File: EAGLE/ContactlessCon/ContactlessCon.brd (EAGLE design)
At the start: 57.1 x 31.4 mm, 5 parts, among them J1 PINHEADER-212*1, J2 PINHEADER-818*1, X1 0446200002

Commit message: Conの配線終了
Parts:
- moved X1 5.06 mm to (30.0, 31.7)
- moved J1 2.00 mm to (6.35, 7.08)
- moved J2 1.43 mm to (53.5, 8.89)
- moved R1 1.00 mm to (28.2, 5.08)
- moved R2 1.00 mm to (28.2, 7.62)
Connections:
- net GPIO: now also X1.5; no longer X1.3
- net SCL: now also X1.4; no longer X1.5
- net SDA: now also X1.3; no longer X1.4
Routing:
- net SDA: track 0.00 -> 48.4 mm
- net SCL: track 0.00 -> 44.0 mm
- net GPIO: track 0.00 -> 40.3 mm
- net SPEAKER: track 0.00 -> 29.1 mm
- net +3V3: track 0.00 -> 22.9 mm
- added copper zone on layer 16, net GND
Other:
- board size 57.1 x 31.4 mm -> 60 x 37.1 mm
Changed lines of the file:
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@@
 <board>
 <plain>
-<wire x1="0" y1="0" x2="57.13" y2="0" width="0" layer="20"/>
-<wire x1="57.13" y1="0" x2="57.13" y2="31.42" width="0" layer="20"/>
-<wire x1="57.13" y1="31.42" x2="0" y2="31.42" width="0" layer="20"/>
-<wire x1="0" y1="31.42" x2="0" y2="0" width="0" layer="20"/>
+<wire x1="0" y1="32.1" x2="0" y2="5" width="0" layer="20"/>
+<wire x1="0" y1="5" x2="5" y2="0" width="0" layer="20" curve="90"/>
+<wire x1="5" y1="0" x2="55" y2="0" width="0" layer="20"/>
+<wire x1="55" y1="0" x2="60" y2="5" width="0" layer="20" curve="90"/>
+<wire x1="60" y1="5" x2="60" y2="32.1" width="0" layer="20"/>
+<wire x1="60" y1="32.1" x2="55" y2="37.1" width="0" layer="20" curve="90"/>
+<wire x1="55" y1="37.1" x2="5" y2="37.1" width="0" layer="20"/>
+<wire x1="5" y1="37.1" x2="0" y2="32.1" width="0" layer="20" curve="90"/>
 </plain>
 <attributes>
@@
 </autorouter>
 <elements>
-<element name="J1" library="PINHEADER" package="PINHEADER-2*1" value="PINHEADER-212*1" x="6.35" y="5.08" smashed="yes" rot="R270">
-<attribute name="NAME" x="8.255" y="7.62" size="1.016" layer="21" font="vector" ratio="15" rot="R270"/>
-</element>
-<element name="J2" library="PINHEADER" package="PINHEADER-8*1" value="PINHEADER-818*1" x="52.07" y="8.89" smashed="yes" rot="R90">
-<attribute name="NAME" x="50.165" y="1.27" size="1.016" layer="25" font="vector" ratio="15" rot="R90"/>
-</element>
-<element name="R1" library="rcl" library_urn="urn:adsk.eagle:library:334" package="R1206" package3d_urn="urn:adsk.eagle:package:23540/2" value="" x="29.21" y="5.08" smashed="yes" rot="R180">
-<attribute name="NAME" x="30.48" y="3.81" size="1.27" layer="25" rot="R180"/>
-<attribute name="POPULARITY" value="41" x="13.97" y="34.29" size="1.778" layer="27" rot="R180" display="off"/>
-<attribute name="SPICEPREFIX" value="R" x="13.97" y="34.29" size="1.778" layer="27" rot="R180" display="off"/>
-<attribute name="VALUE" x="30.48" y="7.62" size="1.27" layer="27" rot="R180"/>
-</element>
-<element name="R2" library="rcl" library_urn="urn:adsk.eagle:library:334" package="R1206" package3d_urn="urn:adsk.eagle:package:23540/2" value="" x="29.21" y="7.62" smashed="yes" rot="R180">
-<attribute name="NAME" x="27.94" y="8.89" size="1.27" layer="25"/>
-<attribute name="POPULARITY" value="41" x="8.89" y="36.83" size="1.778" layer="27" rot="R180" display="off"/>
-<attribute name="SPICEPREFIX" value="R" x="8.89" y="36.83" size="1.778" layer="27" rot="R180" display="off"/>
-<attribute name="VALUE" x="30.48" y="10.16" size="1.27" layer="27" rot="R180"/>
-</element>
-<element name="X1" library="con-molex" library_urn="urn:adsk.eagle:library:165" package="0446200002" package3d_urn="urn:adsk.eagle:package:8078921/1" value="0446200002" x="29.21" y="26.67" smashed="yes" rot="R180">
-<attribute name="MF" value="MOLEX" x="6.35" y="31.75" size="1.778" layer="27" rot="R180" display="off"/>
-<attribute name="MPN" value="0446200002" x="6.35" y="31.75" size="1.778" layer="27" rot="R180" display="off"/>
-<attribute name="NAME" x="36.83" y="15.875" size="1.27" layer="25" rot="R180"/>
-<attribute name="OC_FARNELL" value="9251910" x="6.35" y="31.75" size="1.778" layer="27" rot="R180" display="off"/>
-<attribute name="POPULARITY" value="0" x="6.35" y="31.75" size="1.778" layer="27" rot="R180" display="off"/>
-<attribute name="VALUE" x="35.56" y="19.05" size="1.27" layer="27" rot="R180"/>
+<element name="J1" library="PINHEADER" package="PINHEADER-2*1" value="PINHEADER-212*1" x="6.35" y="7.08" smashed="yes" rot="R270">
+<attribute name="NAME" x="8.255" y="9.62" size="1.016" layer="21" font="vector" ratio="15" rot="R270"/>
+</element>
+<element name="J2" library="PINHEADER" package="PINHEADER-8*1" value="PINHEADER-818*1" x="53.5" y="8.89" smashed="yes" rot="R90">
+<attribute name="NAME" x="51.595" y="1.27" size="1.016" layer="25" font="vector" ratio="15" rot="R90"/>
+</element>
+<element name="R1" library="rcl" library_urn="urn:adsk.eagle:library:334" package="R1206" package3d_urn="urn:adsk.eagle:package:23540/2" value="" x="28.21" y="5.08" smashed="yes" rot="R180">
+<attribute name="NAME" x="29.48" y="3.81" size="1.27" layer="25" rot="R180"/>
+<attribute name="POPULARITY" value="41" x="12.97" y="34.29" size="1.778" layer="27" rot="R180" display="off"/>
+<attribute name="SPICEPREFIX" value="R" x="12.97" y="34.29" size="1.778" layer="27" rot="R180" display="off"/>
+<attribute name="VALUE" x="29.48" y="7.62" size="1.27" layer="27" rot="R180"/>
+</element>
+<element name="R2" library="rcl" library_urn="urn:adsk.eagle:library:334" package="R1206" package3d_urn="urn:adsk.eagle:package:23540/2" value="" x="28.21" y="7.62" smashed="yes" rot="R180">
+<attribute name="NAME" x="26.94" y="8.89" size="1.27" layer="25"/>
+<attribute name="POPULARITY" value="41" x="7.89" y="36.83" size="1.778" layer="27" rot="R180" display="off"/>
+<attribute name="SPICEPREFIX" value="R" x="7.89" y="36.83" size="1.778" layer="27" rot="R180" display="off"/>
+<attribute name="VALUE" x="29.48" y="10.16" size="1.27" layer="27" rot="R180"/>
+</element>
+<element name="X1" library="con-molex" library_urn="urn:adsk.eagle:library:165" package="0446200002" package3d_urn="urn:adsk.eagle:package:8078921/1" value="0446200002" x="30" y="31.67" smashed="yes" rot="R180">
+<attribute name="MF" value="MOLEX" x="7.14" y="36.75" size="1.778" layer="27" rot="R180" display="off"/>
+<attribute name="MPN" value="0446200002" x="7.14" y="36.75" size="1.778" layer="27" rot="R180" display="off"/>
+<attribute name="NAME" x="37.62" y="20.875" size="1.27" layer="25" rot="R180"/>
+<attribute name="OC_FARNELL" value="9251910" x="7.14" y="36.75" size="1.778" layer="27" rot="R180" display="off"/>
+<attribute name="POPULARITY" value="0" x="7.14" y="36.75" size="1.778" layer="27" rot="R180" display="off"/>
+<attribute name="VALUE" x="36.35" y="24.05" size="1.27" layer="27" rot="R180"/>
 </element>
 </elements>
@@
 <contactref element="X1" pad="8"/>
 <contactref element="X1" pad="6"/>
-<wire x1="30.734" y1="22.352" x2="32.766" y2="22.352" width="0" layer="19" extent="1-1"/>
-<wire x1="52.07" y1="20.32" x2="30.734" y2="22.352" width="0" layer="19" extent="1-1"/>
-<wire x1="27.788" y1="5.08" x2="52.07" y2="20.32" width="0" layer="19" extent="1-1"/>
-<wire x1="27.788" y1="7.62" x2="27.788" y2="5.08" width="0" layer="19" extent="1-1"/>
+<wire x1="53.5" y1="20.32" x2="40.588" y2="20.32" width="0.4064" layer="1"/>
+<wire x1="40.588" y1="20.32" x2="33.556" y2="27.352" width="0.4064" layer="1"/>
+<wire x1="31.524" y1="27.352" x2="33.556" y2="27.352" width="0" layer="19" extent="1-1"/>
+<wire x1="26.788" y1="7.62" x2="31.524" y2="27.352" width="0" layer="19" extent="1-1"/>
+<wire x1="26.788" y1="5.08" x2="26.788" y2="7.62" width="0" layer="19" extent="1-1"/>
 </signal>
 <signal name="GND">
@@
 <contactref element="X1" pad="7"/>
 <contactref element="X1" pad="2"/>
-<wire x1="26.67" y1="22.352" x2="31.75" y2="24.13" width="0" layer="19" extent="1-1"/>
-<wire x1="6.35" y1="3.81" x2="26.67" y2="22.352" width="0" layer="19" extent="1-1"/>
-<wire x1="52.07" y1="15.24" x2="6.35" y2="3.81" width="0" layer="19" extent="1-1"/>
-<wire x1="52.07" y1="2.54" x2="52.07" y2="15.24" width="0" layer="19" extent="1-1"/>
+<polygon width="0.127" layer="16" isolate="0.4064">
+<vertex x="3" y="36"/>
+<vertex x="56" y="36"/>
+<vertex x="58" y="34"/>
+<vertex x="58" y="3"/>
+<vertex x="56" y="1"/>
+<vertex x="3" y="1"/>
+<vertex x="1" y="3"/>
+<vertex x="1" y="34"/>
+</polygon>
 </signal>
 <signal name="GPIO">
 <contactref element="J2" pad="5"/>
 <contactref element="J2" pad="4"/>
-<contactref element="X1" pad="3"/>
-<wire x1="52.07" y1="12.7" x2="27.686" y2="24.13" width="0" layer="19" extent="1-1"/>
-<wire x1="52.07" y1="10.16" x2="52.07" y2="12.7" width="0" layer="19" extent="1-1"/>
+<wire x1="53.5" y1="10.16" x2="53.5" y2="12.7" width="0.254" layer="1"/>
+<contactref element="X1" pad="5"/>
+<wire x1="30.508" y1="29.13" x2="30.508" y2="15.492" width="0.254" layer="1"/>
+<wire x1="33.3" y1="12.7" x2="53.5" y2="12.7" width="0.254" layer="1"/>
+<wire x1="30.508" y1="15.492" x2="33.3" y2="12.7" width="0.254" layer="1"/>
 </signal>
 <signal name="SCL">
 <contactref element="J2" pad="3"/>
 <contactref element="R2" pad="1"/>
-<contactref element="X1" pad="5"/>
-<wire x1="52.07" y1="7.62" x2="29.718" y2="24.13" width="0" layer="19" extent="1-1"/>
-<wire x1="30.632" y1="7.62" x2="52.07" y2="7.62" width="0" layer="19" extent="1-1"/>
+<wire x1="29.508" y1="7.744" x2="29.632" y2="7.62" width="0.254" layer="1"/>
+<wire x1="53.5" y1="7.62" x2="30" y2="7.62" width="0.254" layer="1"/>
+<contactref element="X1" pad="4"/>
+<wire x1="30" y1="7.62" x2="29.632" y2="7.62" width="0.254" layer="1"/>
+<wire x1="29.492" y1="27.352" x2="29.492" y2="8.128" width="0.254" layer="1"/>
+<wire x1="29.492" y1="8.128" x2="30" y2="7.62" width="0.254" layer="1"/>
 </signal>
 <signal name="SDA">
 <contactref element="J2" pad="2"/>
 <contactref element="R1" pad="1"/>
-<contactref element="X1" pad="4"/>
-<wire x1="52.07" y1="5.08" x2="30.632" y2="5.08" width="0" layer="19" extent="1-1"/>
-<wire x1="28.702" y1="22.352" x2="52.07" y2="5.08" width="0" layer="19" extent="1-1"/>
+<wire x1="28.492" y1="6.22" x2="28.856" y2="5.856" width="0.254" layer="1"/>
+<wire x1="28.856" y1="5.856" x2="29.632" y2="5.08" width="0.254" layer="1"/>
+<wire x1="29.632" y1="5.08" x2="53.5" y2="5.08" width="0.254" layer="1"/>
+<contactref element="X1" pad="3"/>
+<wire x1="28.476" y1="29.13" x2="28.476" y2="6.236" width="0.254" layer="1"/>
+<wire x1="28.476" y1="6.236" x2="28.492" y2="6.22" width="0.254" layer="1"/>
 </signal>
 <signal name="SPEAKER">
 <contactref element="J1" pad="1"/>
 <contactref element="X1" pad="1"/>
-<wire x1="6.35" y1="6.35" x2="25.654" y2="24.13" width="0" layer="19" extent="1-1"/>
+<wire x1="6.35" y1="8.35" x2="26.444" y2="28.444" width="0.254" layer="1"/>
+<wire x1="26.444" y1="28.444" x2="26.444" y2="29.13" width="0.254" layer="1"/>
 </signal>
 </signals>

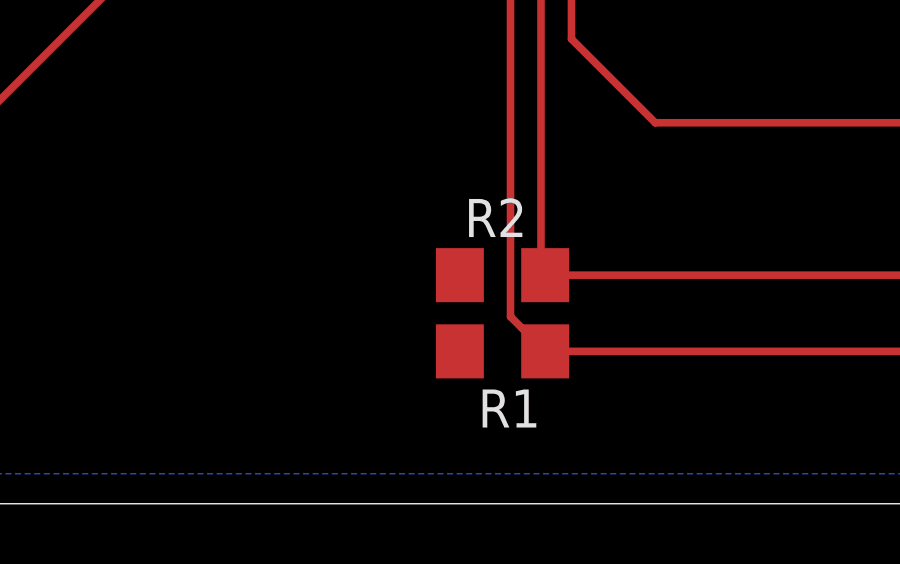
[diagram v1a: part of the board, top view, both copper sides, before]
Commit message: 抵抗のvalueを追加
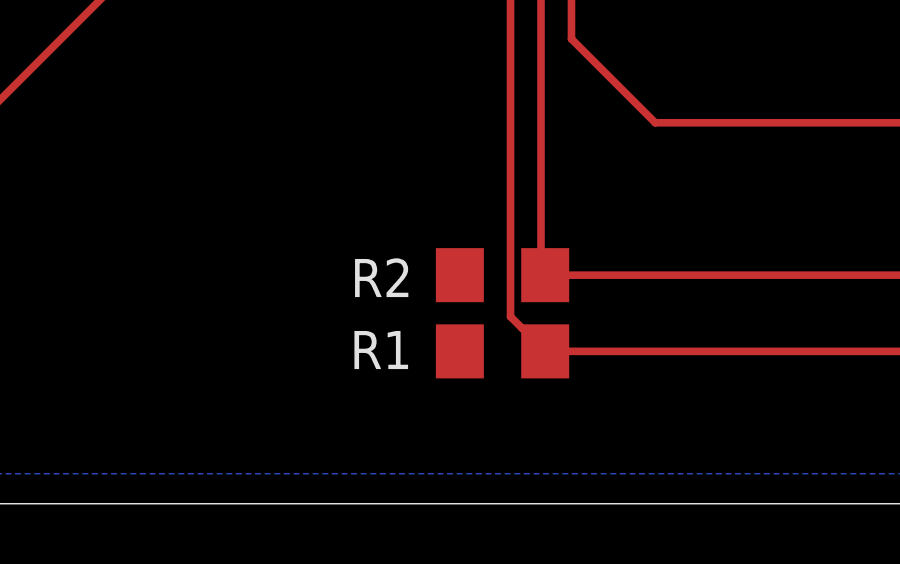
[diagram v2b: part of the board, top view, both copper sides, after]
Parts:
- R1, R2: value (none) -> 1k
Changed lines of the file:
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@@
 <attribute name="NAME" x="51.595" y="1.27" size="1.016" layer="25" font="vector" ratio="15" rot="R90"/>
 </element>
-<element name="R1" library="rcl" library_urn="urn:adsk.eagle:library:334" package="R1206" package3d_urn="urn:adsk.eagle:package:23540/2" value="" x="28.21" y="5.08" smashed="yes" rot="R180">
-<attribute name="NAME" x="29.48" y="3.81" size="1.27" layer="25" rot="R180"/>
+<element name="R1" library="rcl" library_urn="urn:adsk.eagle:library:334" package="R1206" package3d_urn="urn:adsk.eagle:package:23540/2" value="1k" x="28.21" y="5.08" smashed="yes" rot="R180">
+<attribute name="NAME" x="23.12" y="4.49" size="1.27" layer="25"/>
 <attribute name="POPULARITY" value="41" x="12.97" y="34.29" size="1.778" layer="27" rot="R180" display="off"/>
 <attribute name="SPICEPREFIX" value="R" x="12.97" y="34.29" size="1.778" layer="27" rot="R180" display="off"/>
-<attribute name="VALUE" x="29.48" y="7.62" size="1.27" layer="27" rot="R180"/>
 </element>
-<element name="R2" library="rcl" library_urn="urn:adsk.eagle:library:334" package="R1206" package3d_urn="urn:adsk.eagle:package:23540/2" value="" x="28.21" y="7.62" smashed="yes" rot="R180">
-<attribute name="NAME" x="26.94" y="8.89" size="1.27" layer="25"/>
+<element name="R2" library="rcl" library_urn="urn:adsk.eagle:library:334" package="R1206" package3d_urn="urn:adsk.eagle:package:23540/2" value="1k" x="28.21" y="7.62" smashed="yes" rot="R180">
+<attribute name="NAME" x="23.14" y="6.89" size="1.27" layer="25"/>
 <attribute name="POPULARITY" value="41" x="7.89" y="36.83" size="1.778" layer="27" rot="R180" display="off"/>
 <attribute name="SPICEPREFIX" value="R" x="7.89" y="36.83" size="1.778" layer="27" rot="R180" display="off"/>
-<attribute name="VALUE" x="29.48" y="10.16" size="1.27" layer="27" rot="R180"/>
 </element>
 <element name="X1" library="con-molex" library_urn="urn:adsk.eagle:library:165" package="0446200002" package3d_urn="urn:adsk.eagle:package:8078921/1" value="0446200002" x="30" y="31.67" smashed="yes" rot="R180">
